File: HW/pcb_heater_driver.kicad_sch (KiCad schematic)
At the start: 0 parts

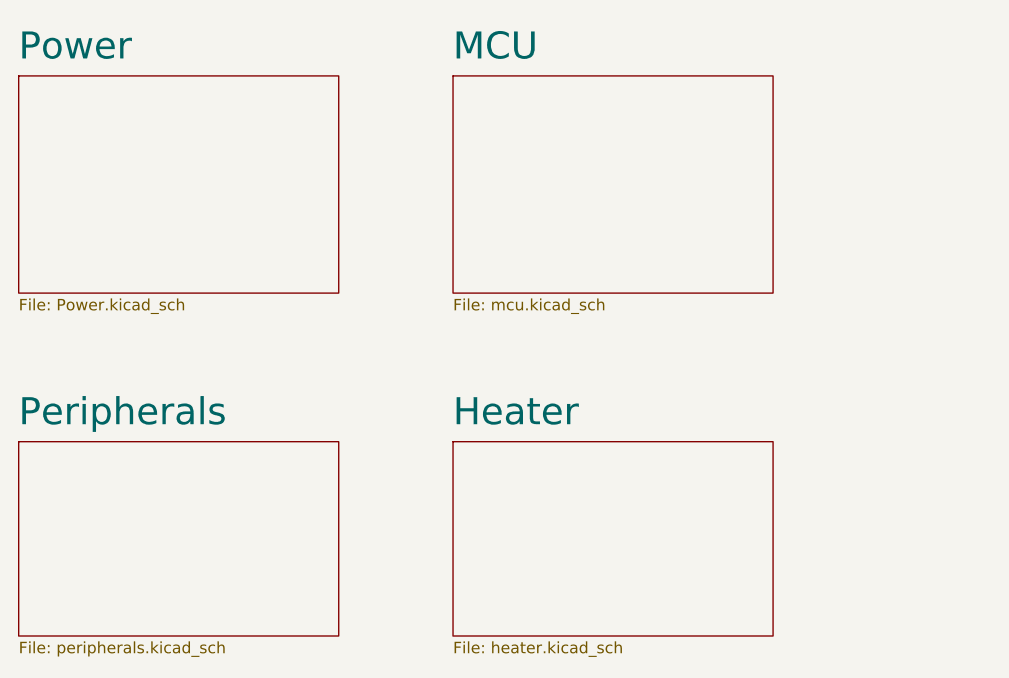
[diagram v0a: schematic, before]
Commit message: QOL changes on pcb, fixed wrong ACDC brick polarity xD
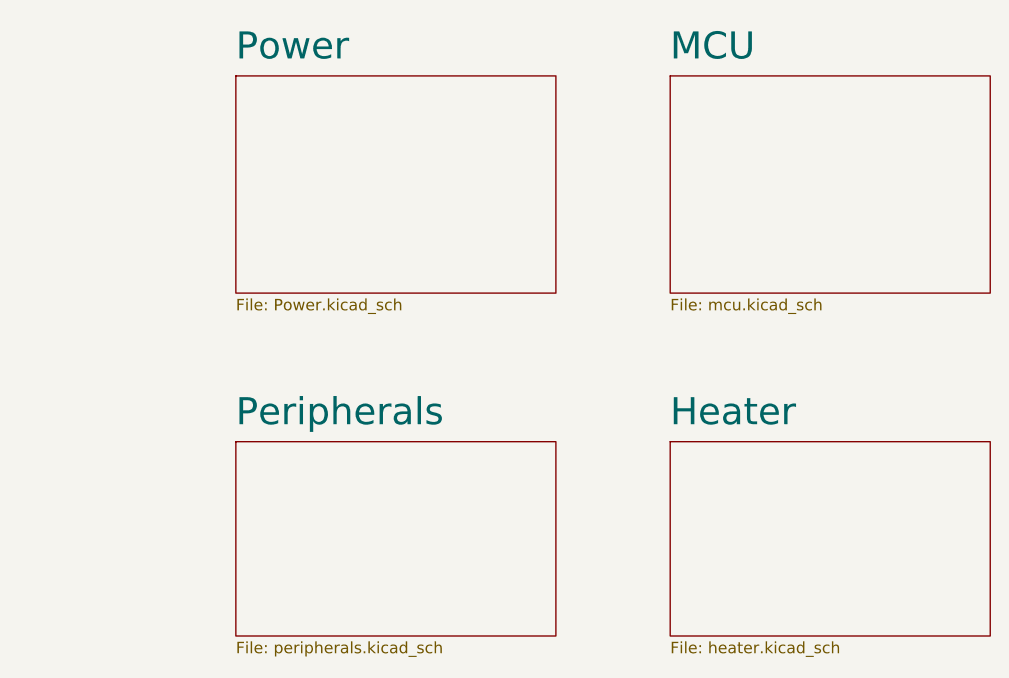
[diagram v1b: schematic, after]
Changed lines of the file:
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@@
     (rev "0")
   )
-  (sheet (at 130.81 71.12) (size 35.56 24.13) (fields_autoplaced)
+  (sheet (at 154.94 71.12) (size 35.56 24.13) (fields_autoplaced)
     (stroke (width 0.1524) (type solid) (color 0 0 0 0))
     (fill (color 0 0 0 0.0000))
-    (property "Sheet name" "MCU" (id 0) (at 130.81 69.5434 0)
+    (property "Sheet name" "MCU" (id 0) (at 154.94 69.5434 0)
       (effects (font (size 3 3)) (justify left bottom))
     )
-    (property "Sheet file" "mcu.kicad_sch" (id 1) (at 130.81 95.8346 0)
+    (property "Sheet file" "mcu.kicad_sch" (id 1) (at 154.94 95.8346 0)
       (effects (font (size 1.27 1.27)) (justify left top))
     )
   )
-  (sheet (at 130.81 111.76) (size 35.56 21.59) (fields_autoplaced)
+  (sheet (at 154.94 111.76) (size 35.56 21.59) (fields_autoplaced)
     (stroke (width 0.1524) (type solid) (color 0 0 0 0))
     (fill (color 0 0 0 0.0000))
-    (property "Sheet name" "Heater" (id 0) (at 130.81 110.1834 0)
+    (property "Sheet name" "Heater" (id 0) (at 154.94 110.1834 0)
       (effects (font (size 3 3)) (justify left bottom))
     )
-    (property "Sheet file" "heater.kicad_sch" (id 1) (at 130.81 133.9346 0)
+    (property "Sheet file" "heater.kicad_sch" (id 1) (at 154.94 133.9346 0)
       (effects (font (size 1.27 1.27)) (justify left top))
     )
   )
-  (sheet (at 82.55 111.76) (size 35.56 21.59) (fields_autoplaced)
+  (sheet (at 106.68 111.76) (size 35.56 21.59) (fields_autoplaced)
     (stroke (width 0.1524) (type solid) (color 0 0 0 0))
     (fill (color 0 0 0 0.0000))
-    (property "Sheet name" "Peripherals" (id 0) (at 82.55 110.1834 0)
+    (property "Sheet name" "Peripherals" (id 0) (at 106.68 110.1834 0)
       (effects (font (size 3 3)) (justify left bottom))
     )
-    (property "Sheet file" "peripherals.kicad_sch" (id 1) (at 82.55 133.9346 0)
+    (property "Sheet file" "peripherals.kicad_sch" (id 1) (at 106.68 133.9346 0)
       (effects (font (size 1.27 1.27)) (justify left top))
     )
   )
-  (sheet (at 82.55 71.12) (size 35.56 24.13) (fields_autoplaced)
+  (sheet (at 106.68 71.12) (size 35.56 24.13) (fields_autoplaced)
     (stroke (width 0.1524) (type solid) (color 0 0 0 0))
     (fill (color 0 0 0 0.0000))
-    (property "Sheet name" "Power" (id 0) (at 82.55 69.5434 0)
+    (property "Sheet name" "Power" (id 0) (at 106.68 69.5434 0)
       (effects (font (size 3 3)) (justify left bottom))
     )
-    (property "Sheet file" "Power.kicad_sch" (id 1) (at 82.55 95.8346 0)
+    (property "Sheet file" "Power.kicad_sch" (id 1) (at 106.68 95.8346 0)
       (effects (font (size 1.27 1.27)) (justify left top))
     )
@@
       (reference "#PWR0122") (unit 1) (value "GND") (footprint "")
     )
+    (path "/d8f51e65-ca8c-412e-9c09-61e73d04032d/b2ac66fc-dea3-4696-bc8f-d9148d41c51c"
+      (reference "#PWR0123") (unit 1) (value "GND") (footprint "")
+    )
+    (path "/7d8672ff-8c9b-4cfe-8dbb-3ae8b2afedd8/122b5dca-3917-40a7-9684-41c0803b0811"
+      (reference "#PWR0124") (unit 1) (value "GND") (footprint "")
+    )
     (path "/d8f51e65-ca8c-412e-9c09-61e73d04032d/bb76d7e0-0d4f-4d41-8360-0ab29495ced5"
       (reference "#PWR0128") (unit 1) (value "GND") (footprint "")
@@
       (reference "D2") (unit 1) (value "RED") (footprint "LED_SMD:LED_0603_1608Metric")
     )
+    (path "/7d8672ff-8c9b-4cfe-8dbb-3ae8b2afedd8/b36f7a51-7fc9-4dcf-982f-9f2874a3c642"
+      (reference "D3") (unit 1) (value "RED") (footprint "LED_SMD:LED_0603_1608Metric")
+    )
     (path "/d5060ff5-86f5-4681-be53-c236c782c8a7/855b6e1d-7d70-4534-8cdd-d0259a8a0142"
       (reference "D4") (unit 1) (value "PRTR5V0U2X") (footprint "Package_TO_SOT_SMD:SOT-143")
@@
     )
     (path "/b389637b-c3c6-4117-a6e9-91a2ebc82014/deda6d3e-4c97-4d01-86a8-1cb7bde9addb"
-      (reference "R10") (unit 1) (value "100k") (footprint "Resistor_SMD:R_0603_1608Metric")
+      (reference "R10") (unit 1) (value "22k") (footprint "Resistor_SMD:R_0603_1608Metric")
     )
     (path "/b389637b-c3c6-4117-a6e9-91a2ebc82014/dc72ae8b-3f09-4409-92cd-78a4bbab9662"
-      (reference "R11") (unit 1) (value "37k") (footprint "Resistor_SMD:R_0603_1608Metric")
+      (reference "R11") (unit 1) (value "5k1") (footprint "Resistor_SMD:R_0603_1608Metric")
     )
     (path "/b389637b-c3c6-4117-a6e9-91a2ebc82014/2b2a43cb-e8f2-47be-b245-c6b5f863b4db"
@@
       (reference "R16") (unit 1) (value "10k") (footprint "Resistor_SMD:R_0603_1608Metric")
     )
+    (path "/b389637b-c3c6-4117-a6e9-91a2ebc82014/07b29739-f4d4-485c-ab03-7f3ae065db9b"
+      (reference "R17") (unit 1) (value "TBD") (footprint "Resistor_SMD:R_0603_1608Metric")
+    )
+    (path "/7d8672ff-8c9b-4cfe-8dbb-3ae8b2afedd8/7e03442e-c2ed-45f2-a63e-c80e79234444"
+      (reference "R18") (unit 1) (value "1k") (footprint "Resistor_SMD:R_0603_1608Metric")
+    )
     (path "/d5060ff5-86f5-4681-be53-c236c782c8a7/d78f8059-f0db-41c1-af68-e8edb59a9047"
       (reference "R19") (unit 1) (value "10k") (footprint "Resistor_SMD:R_0603_1608Metric")
@@
     )
     (path "/b389637b-c3c6-4117-a6e9-91a2ebc82014/36dad684-14a6-4fa8-a60b-38b9d5c41886"
-      (reference "TH1") (unit 1) (value "Heater_1") (footprint "TestPoint:TestPoint_2Pads_Pitch2.54mm_Drill0.8mm")
+      (reference "TH1") (unit 1) (value "Heater_1") (footprint "Jumper:SolderJumper-2_P1.3mm_Open_RoundedPad1.0x1.5mm")
     )
     (path "/b389637b-c3c6-4117-a6e9-91a2ebc82014/92251fe2-af60-40b0-8d5b-016c827aa918"
-      (reference "TH2") (unit 1) (value "Heater_2") (footprint "TestPoint:TestPoint_2Pads_Pitch2.54mm_Drill0.8mm")
+      (reference "TH2") (unit 1) (value "Heater_2") (footprint "Jumper:SolderJumper-2_P1.3mm_Open_RoundedPad1.0x1.5mm")
     )
     (path "/b389637b-c3c6-4117-a6e9-91a2ebc82014/d6231291-1ddc-4f8a-b861-15aa16195f01"
-      (reference "TH3") (unit 1) (value "Heater_3") (footprint "TestPoint:TestPoint_2Pads_Pitch2.54mm_Drill0.8mm")
+      (reference "TH3") (unit 1) (value "Heater_3") (footprint "Jumper:SolderJumper-2_P1.3mm_Open_RoundedPad1.0x1.5mm")
     )
     (path "/b389637b-c3c6-4117-a6e9-91a2ebc82014/0a720116-f99e-41d0-ba4c-69a9b7e14b24"
-      (reference "TH4") (unit 1) (value "mosfet") (footprint "TestPoint:TestPoint_2Pads_Pitch2.54mm_Drill0.8mm")
+      (reference "TH4") (unit 1) (value "mosfet") (footprint "Jumper:SolderJumper-2_P1.3mm_Open_RoundedPad1.0x1.5mm")
     )
     (path "/7d8672ff-8c9b-4cfe-8dbb-3ae8b2afedd8/39757241-0951-4c4d-a6c3-1fb3ba34292c"
@@
       (reference "U5") (unit 1) (value "fork_p5.0mm") (footprint "fork_connector_p5.0mm:fork_p5.0mm")
     )
-  )
+    (path "/d8f51e65-ca8c-412e-9c09-61e73d04032d/8bec05cb-ebfd-4afb-9364-60e211f8239f"
+      (reference "U6") (unit 1) (value "fork_p5.0mm") (footprint "fork_connector_p5.0mm:fork_p5.0mm")
+    )
+  )
